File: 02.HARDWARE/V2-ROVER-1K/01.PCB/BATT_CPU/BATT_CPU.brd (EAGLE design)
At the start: 33 x 44.3 mm, 68 parts, among them J1 2314820-6, K3 FLEX_CONN, K4 FLEX6, K5 FLEX8, U1 ATSAMD21G18_QFN, U2 TPS78230DDCR, U3 TPS78230DDCR, U5 MAX9062EUK+T, U6 MAX9062EUK+T, U7 MCP6071T-E/OT, U8 SN74LVC1G19DBVR, X2 32.768

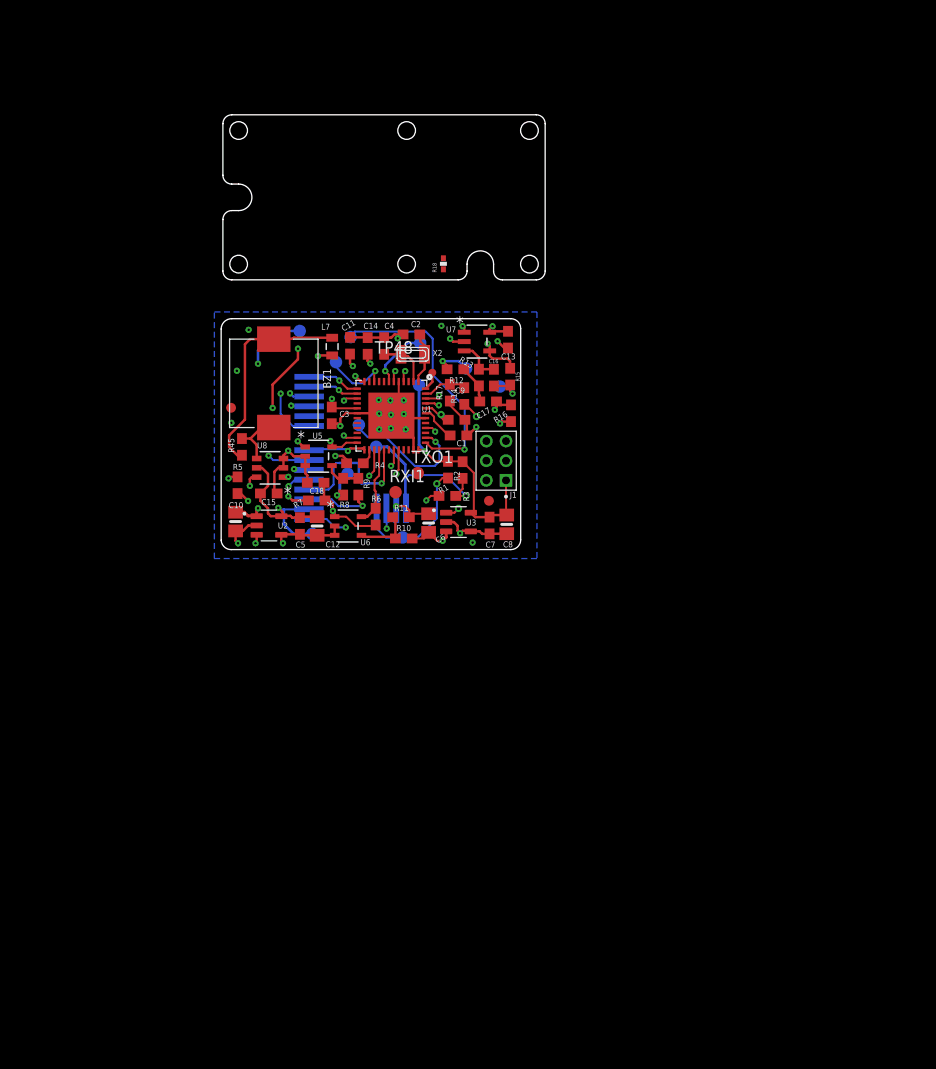
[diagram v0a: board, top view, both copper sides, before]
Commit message: Trabajo dia 31 Oct. Update
SOLO TRABAJO SOBRE ESQUEMATICO.
- Inclusion pantalla 49".
- Cambio en el diseño de la gestion de la laimentacion. Inclusion de transistor P comandado por 2 N (Boton de encendido y Señal digital CPU)
- Multiplaxado del control del DCDC y del Switch de salida, entre las señales digitales de la CPU y el comparador.
- Se añaden fajas place holder.
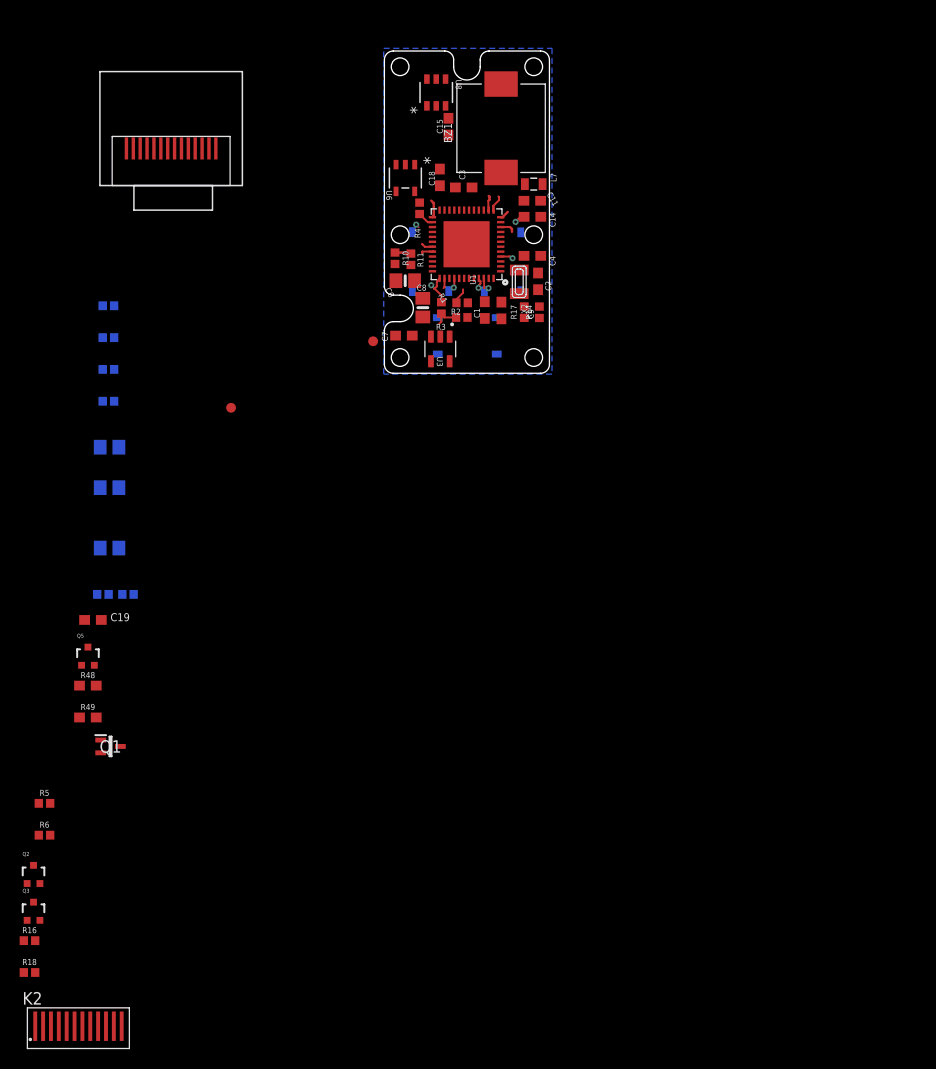
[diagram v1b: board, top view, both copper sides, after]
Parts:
- removed C10, C12: 2.2uF, microbuilder:0805-NO
- removed C5: 100n, microbuilder:0603-NO
- removed GND, IOSENSE, ISENSE_RAW, RXI, RXI1, SCL_2, SDA_2, TST_MODE, TXO, TXO1, VBUS, VCC, VCC_2, VOUTSENSE: TESTPAD_TPSQB1,27, BeagleBone_Blue_R3:TESTPAD_B1,27
- removed J1: 2314820-6, connector 2x3-2mm:TE_2314820-6
- removed K3: FLEX_CONN, Flex_3mm:FLEX4
- removed K4: FLEX6, Flex_3mm:FLEX6
- removed K5: FLEX8, Flex_3mm:FLEX8
- removed R45: 330, SparkFun-Resistors:0603
- removed TP48: TPTP08R, testpad:TP08R
- removed U2: TPS78230DDCR, TPS78230DDCR:SOT95P280X110-5N
- removed U5: MAX9062EUK+T, MAX9062:21-0057F_MXM
- removed U7: MCP6071T-E/OT, MCP6071:SOT-23-5_MC_MCH
- added C19: 100n, microbuilder:0603-NO
- added K2: FLEX6, Flex:FLEX6
- added Q1: BSS84W-7-F, BSS84W-7-F:SOT65P222X110-3N
- added Q2, Q3, Q5: 2N7002PW, SparkFun-DiscreteSemi:SOT323
- added R48: 100R, SparkFun-Resistors:0603
- added R49: 10k, SparkFun-Resistors:0603
- added S1, S2, S3: PTS526_SKG15_SMTR2_LFS, PTS526_SKG15_SMTR2_LFS:PTS526SKG15SMTR2LFS
- added U$30: 64X32_OLED_049, OLED 66 64x48:LCD_14_PINS
- C13: device microbuilder:0603-NO -> rcl:C0805
- C16, C17: value 1u -> 100n; device microbuilder:0603-NO -> rcl:C0805
- R1, R10, R14, R17, R2, R3, R4: device SparkFun-Resistors:0603 -> SparkFun-Resistors:0402
- R11: value 8.2k -> 8k2; device SparkFun-Resistors:0603 -> SparkFun-Resistors:0402
- R12: value 2.4k -> 2k2; device SparkFun-Resistors:0603 -> SparkFun-Resistors:0402
- R13: value 62k -> 100R; device SparkFun-Resistors:0603 -> SparkFun-Resistors:0402
- R15: value 2.4k -> 100R; device SparkFun-Resistors:0603 -> SparkFun-Resistors:0402
- R16: value 36k -> (none); device SparkFun-Resistors:0603 -> SparkFun-Resistors:0402
- R18: value RESISTOR0402 -> (none); device BeagleBone_Blue_R3:0402-RES -> SparkFun-Resistors:0402
- R5: value 100k -> (none); device SparkFun-Resistors:0603 -> SparkFun-Resistors:0402
- R6: value 10k -> (none); device SparkFun-Resistors:0603 -> SparkFun-Resistors:0402
- R7: value 10k -> 2k2; device SparkFun-Resistors:0603 -> SparkFun-Resistors:0402
- R8: value 120k -> 100R; device SparkFun-Resistors:0603 -> SparkFun-Resistors:0402
- R9: value 5.6k -> 2k2; device SparkFun-Resistors:0603 -> SparkFun-Resistors:0402
- moved R18 83.5 mm to (4.55, -36.4), turned to 0 degrees
- moved R16 72.7 mm to (4.55, -33.2), turned to 0 degrees
- moved R15 47.0 mm to (12.0, 2.08), flipped to the bottom, turned to 0 degrees
- moved R6 46.8 mm to (6.08, -22.4), turned to 0 degrees
- moved C13 42.0 mm to (12.7, 17.1), flipped to the bottom, turned to 0 degrees
- moved U8 41.8 mm to (46.0, 53.2), turned to 90 degrees
- moved C15 41.6 mm to (47.2, 49.7), turned to 270 degrees
- moved C17 41.3 mm to (12.7, 6.79), flipped to the bottom
- moved C16 40.7 mm to (12.7, 12.9), flipped to the bottom, turned to 0 degrees
- moved R5 37.9 mm to (6.08, -19.2), turned to 0 degrees
- moved R13 37.8 mm to (12.6, 21.7), flipped to the bottom, turned to 0 degrees
- moved U6 35.9 mm to (42.8, 44.5), turned to 270 degrees
- moved R12 35.3 mm to (12.6, 25.0), flipped to the bottom, turned to 0 degrees
- moved BZ1 34.8 mm to (52.6, 49.5), turned to 90 degrees
- moved C18 33.6 mm to (46.3, 44.5), turned to 90 degrees
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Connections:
- removed net #EN_DCDC: K5.9, U1.25
- removed net /FLAG_BATTLOW: R6.1, U1.28, U6.5
- removed net D+: U1.34
- removed net D-: U1.33
- removed net EN_VCC2: R5.2, U1.15, U2.3
- removed net FLAG_CHRG: R7.1, U1.24, U5.5
- removed net ISENSE_RAW: ISENSE_RAW.TP, K5.5, R12.2
- removed net N$11: R8.1, R9.1, U5.4
- removed net N$12: U1.39
- removed net N$14: U1.41
- removed net N$15: TP48.TP, U1.48
- removed net N$4: U1.11
- removed net N$8: C17.1, R12.1, R13.2
- removed net OP_SWITCH: K5.4, U1.29
- removed net SCL2_CPU: R4.2, U1.26
- removed net SCL_2: K3.4, R1.1, R4.1, SCL_2.TP
- removed net SDA2_CPU: R3.2, U1.27
- removed net SDA_2: K3.1, R2.1, R3.1, SDA_2.TP
- removed net USB_SEL: U1.30
- removed net VCC_2: C12.1, C13.1, C15.1, C5.1, K4.1, K5.2, U2.5, U7.5, U8.5, VCC_2.TP
- new net CPU_EN_OUT: R18.2, U1.25
- new net EN_OUT: K2.4, Q5.3, R18.1
- new net EN_VCC: Q3.1, R16.2, U1.15
- new net IN_OVC: Q5.1, R48.2, R49.2
- new net N$2: C13.1, R8.2, R9.2, S1.2
- new net N$3: C16.1, R12.2, R13.1, S2.2
- new net N$58: R48.1, U6.5
- new net N$6: Q1.1, Q2.3, Q3.3, R5.2
- new net SCL_CPU: R4.2, U1.32
- new net SDA_CPU: R3.2, U1.31
- new net S_POWER: Q2.1, R15.2, R6.2
- net !RESET: now also K2.10; no longer J1.3
- net GND: now also C17.2, C19.2, K2.2, Q2.2, Q3.2, Q5.2, R16.1, R49.1, R6.1, S1.4, S2.4, S3.4; no longer C10.2, C12.2, C5.2, GND.TP, J1.5, K3.2, K4.2, K5.3, R15.2, R5.1, R9.2, U2.2, U2.4, U5.2, U5.3, U7.2
- net IOSENSE: now also K2.8; no longer C17.2, IOSENSE.TP, R16.1, U7.1
- net N$1: now also C17.1, R7.2, S3.2; no longer R16.2, U7.4
- net N$10: now also C19.1
- net N$13: now also C6.1, Q1.2, U3.1, U3.3; no longer C16.1, R13.1, U7.3
- net N$19: no longer R45.1
- net N$22: no longer R45.2
- net RXI: now also K2.7; no longer RXI.TP, RXI1.TP
- net SCL: now also R1.1, R4.1; no longer K4.4, K5.7, U1.32
- net SDA: now also R2.1, R3.1; no longer K4.3, K5.1, U1.31
- net SWCLK: now also K2.6; no longer J1.4
- net SWDIO: now also K2.5; no longer J1.2
- net S_DOWN: now also R13.2; no longer K4.6
- net S_UP: now also R8.1; no longer K4.5
- net TST_MODE: no longer TST_MODE.TP
- net TXO: no longer TXO.TP, TXO1.TP
- net VBUS: now also K2.3, Q1.3, R5.1, R7.1; no longer C10.1, C6.1, K3.3, R8.2, U2.1, U3.1, U3.3, VBUS.TP
- net VCC: now also C15.1, K2.1, R12.1, R9.1, U8.5; no longer J1.1, R6.2, R7.2, U5.1, VCC.TP
- net VOUTSENSE: now also K2.9; no longer K5.8, VOUTSENSE.TP
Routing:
- net GND: track 77.5 -> 0.00 mm, vias 27 -> 0
- net VCC: track 45.6 -> 0.00 mm, vias 7 -> 0
- net ISENSE_RAW: track 41.5 -> 0.00 mm, vias 4 -> 0
- net SDA_CPU: track 0.00 -> 37.5 mm, vias 0 -> 2
- net SCL_2: track 28.9 -> 0.00 mm, vias 2 -> 0
- net VCC_2: track 28.4 -> 0.00 mm, vias 3 -> 0
- net SDA: track 30.5 -> 2.84 mm, vias 3 -> 0
- net TXO: track 25.7 -> 1.32 mm, vias 1 -> 0
- net SCL_CPU: track 0.00 -> 23.8 mm
- net EN_VCC2: track 23.2 -> 0.00 mm, vias 3 -> 0
- net N$19: track 21.9 -> 0.00 mm
- net SDA_2: track 21.5 -> 0.00 mm, vias 1 -> 0
- net EN_VCC: track 0.00 -> 19.4 mm
- net VBUS: track 64.1 -> 47.3 mm, vias 6 -> 0
- net OP_SWITCH: track 15.1 -> 0.00 mm, vias 1 -> 0
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- removed copper zone on layer 2, net VCC_2
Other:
- board size 33 x 44.3 mm -> 16.8 x 32.8 mm
- board text removed: "BATT_CPU v5 Nov21"

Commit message: Modificacion Ruteado CPU
Se añade la version 1 de las dimensiones del PCB y se posicionan los componentes sin ruteado.
FALTA: Circuito acondicionamiento Display .
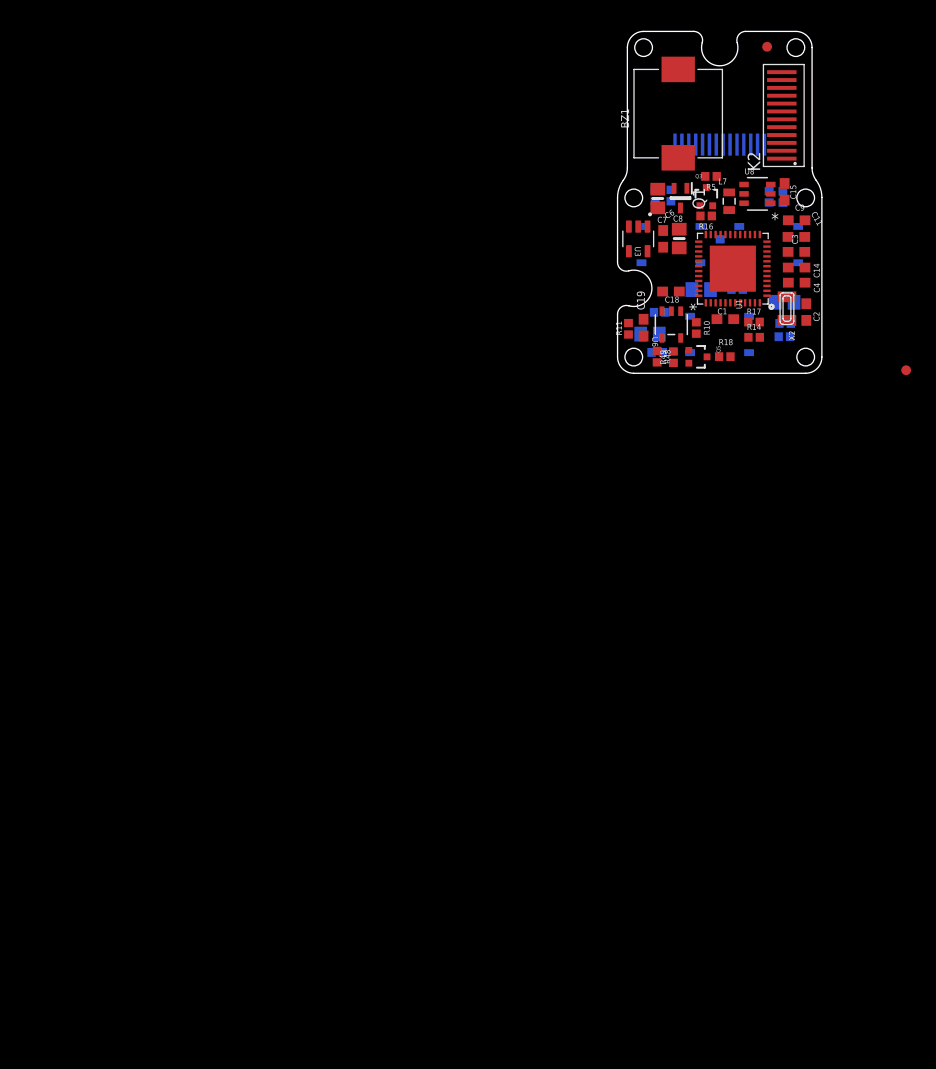
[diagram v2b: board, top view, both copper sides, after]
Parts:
- removed Q2: 2N7002PW, SparkFun-DiscreteSemi:SOT323
- removed R6: (no value), SparkFun-Resistors:0402
- R48: device SparkFun-Resistors:0603 -> SparkFun-Resistors:0402
- R49: value 10k -> 10K; device SparkFun-Resistors:0603 -> SparkFun-Resistors:0402
- moved K2 116.5 mm to (80.9, 48.9), turned to 90 degrees
- moved R16 100.9 mm to (73.4, 40.6), turned to 180 degrees
- moved Q3 99.9 mm to (73.4, 42.6)
- moved R18 94.5 mm to (75.3, 26.3)
- moved R5 93.1 mm to (73.9, 44.6), turned to 180 degrees
- moved Q1 80.5 mm to (70.8, 42.4), turned to 270 degrees
- moved C16 71.3 mm to (81.4, 31.8), turned to 180 degrees
- moved R49 70.0 mm to (70.1, 26.2), turned to 90 degrees
- moved Q5 69.2 mm to (72.6, 26.3), turned to 270 degrees
- moved R13 69.1 mm to (81.4, 28.3), turned to 180 degrees
- moved R12 69.0 mm to (81.5, 29.7)
- moved U$35 68.8 mm to (93.8, 24.9)
- moved R48 66.9 mm to (68.4, 26.3), turned to 270 degrees
- moved U$30 64.9 mm to (79.4, 46.7), flipped to the bottom
- moved R8 64.0 mm to (76.6, 33.1)
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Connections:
- net CPU_EN_OUT renamed CPU_EN_DCDC
- net EN_OUT renamed EN_DCDC
- net EN_VCC renamed EN_VCC_2
- removed net N$13: C6.1, Q1.2, U3.1, U3.3
- new net N$4: U1.26
- new net OP_SWITCH: K2.11
- new net VCC_2: K2.12, Q1.2
- net GND: no longer Q2.2, R6.1
- net N$6: no longer Q2.3
- net S_POWER: no longer Q2.1, R6.2
- net VBUS: now also C6.1, U3.1, U3.3; no longer Q1.3, R5.1
- net VCC: now also Q1.3, R5.1
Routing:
- net VBUS: track 47.3 -> 0.00 mm
- net SDA_CPU: track 37.5 -> 0.00 mm, vias 2 -> 0
- net VOUTSENSE: track 23.9 -> 0.00 mm
- net SCL_CPU: track 23.8 -> 0.00 mm
- net N$17: track 21.1 -> 0.00 mm
- net EN_VCC_2: track 19.4 -> 0.00 mm
- net IOSENSE: track 18.8 -> 0.00 mm
- net SWDIO: track 16.7 -> 0.00 mm, vias 1 -> 0
- net SCL: track 14.9 -> 0.00 mm
- net !RESET: track 13.8 -> 0.00 mm, vias 1 -> 0
- net TST_MODE: track 11.9 -> 0.00 mm
- net BUZZER: track 8.86 -> 0.00 mm
- net SWCLK: track 6.44 -> 0.00 mm, vias 1 -> 0
- net AREF: track 6.19 -> 0.00 mm, vias 2 -> 0
- net SDA: track 2.84 -> 0.00 mm
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- removed copper zone on layer 15, net GND
- removed copper zone on layer 16, net GND
- removed copper zone on layer 2, net GND
- removed copper zone on layer 2, net VCC
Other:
- board size 16.8 x 32.8 mm -> 20.8 x 34.8 mm

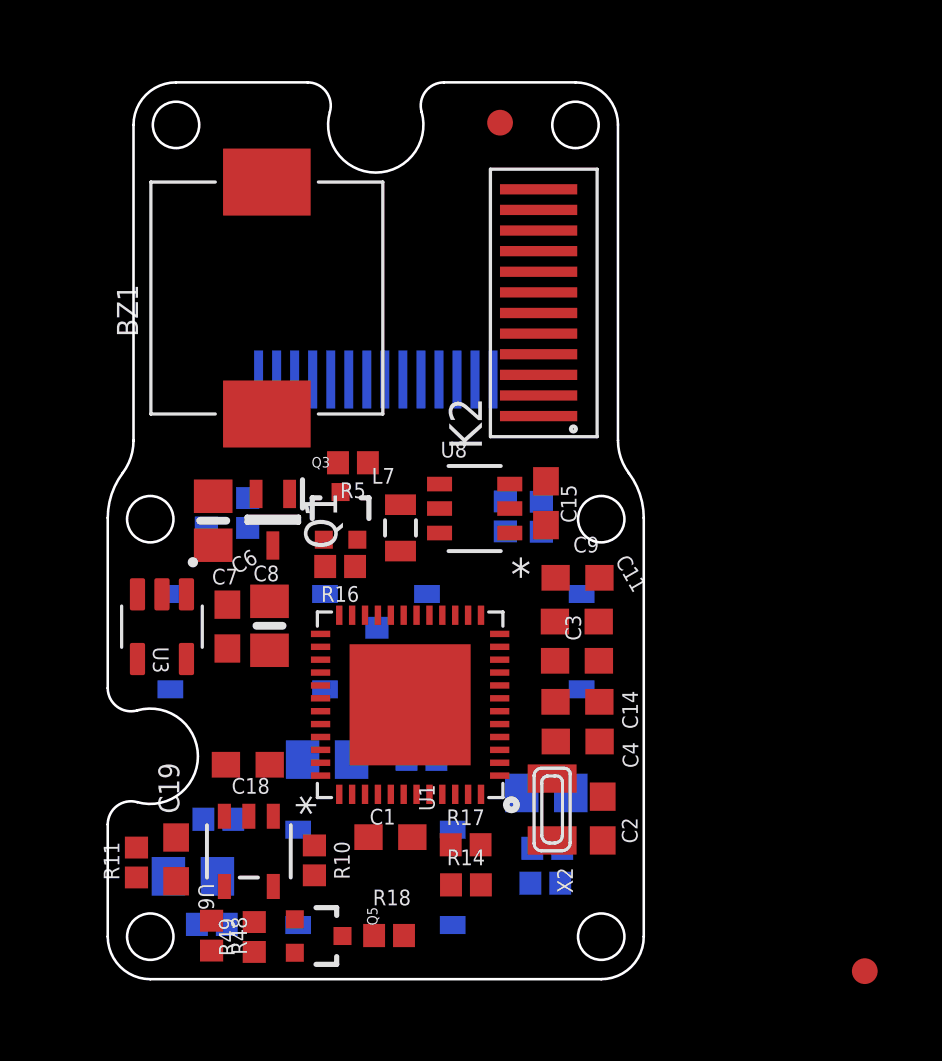
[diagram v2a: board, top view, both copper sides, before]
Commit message: Update CPU PCB.
Routeado terminado v1. PENDIENTE DE REVISION.
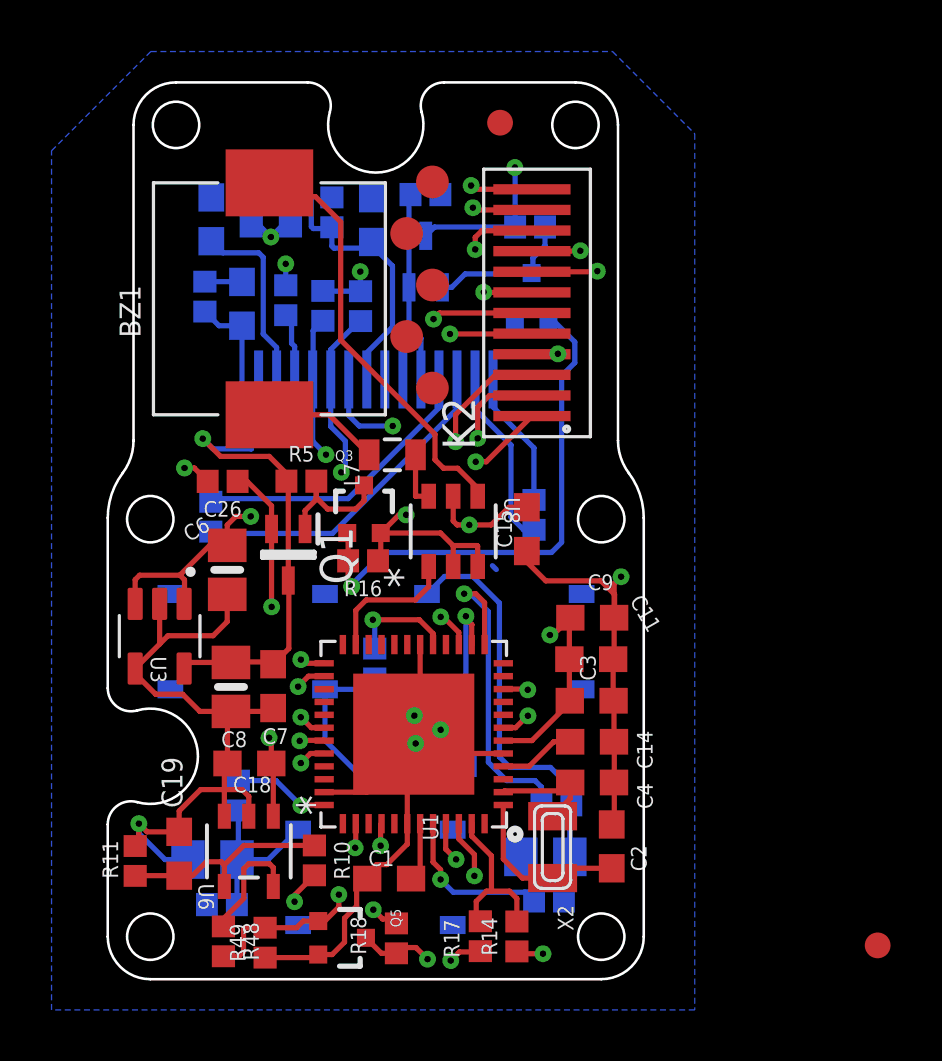
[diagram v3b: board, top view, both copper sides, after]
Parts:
- added C10, C24, C25, C26, C5: 0.1uF, SparkFun-Capacitors:0402
- added C12, C23: 1.0uF, SparkFun-Capacitors:0402
- added C20: 2.2uF, SparkFun-Capacitors:0603
- added C21, C22: 4.7uF, SparkFun-Capacitors:0603
- added Q2: BSS84W-7-F, BSS84W-7-F:SOT65P222X110-3N
- added Q4: 2N7002PW, SparkFun-DiscreteSemi:SOT323
- added R6: 4K7, SparkFun-Resistors:0402
- added VBUS, VBUS1, VBUS2, VBUS3, VBUS4: TESTPAD_TPSQB1,27, BeagleBone_Blue_R3:TESTPAD_B1,27
- R1, R2: value 2k2 -> 4K7
- R3: value 100R -> 560K
- R4: value 100R -> (none)
- moved R4 15.6 mm to (80.8, 53.8), turned to 180 degrees
- moved R3 12.0 mm to (71.3, 50.9), turned to 270 degrees
- moved R2 11.8 mm to (72.8, 50.7)
- moved R1 10.00 mm to (74.2, 50.7)
- moved R7 5.11 mm to (69.5, 31.7), turned to 270 degrees
- moved R17 3.60 mm to (78.9, 26.2), turned to 90 degrees
- moved R15 3.31 mm to (68.8, 27.5)
- moved R13 3.08 mm to (81.8, 31.4), turned to 0 degrees
- moved C7 2.92 mm to (70.8, 36.0), turned to 270 degrees
- moved L7 2.85 mm to (75.5, 44.9), turned to 180 degrees
- moved R14 2.81 mm to (80.3, 26.2), turned to 90 degrees
- moved C8 2.80 mm to (69.2, 35.9), turned to 270 degrees
- moved C16 2.48 mm to (81.4, 29.3), turned to 0 degrees
- moved R5 2.13 mm to (71.9, 43.9), turned to 0 degrees
- moved R12 2.04 mm to (81.5, 27.6), turned to 180 degrees
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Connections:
- removed net IN_OVC: Q5.1, R48.2, R49.2
- removed net SCL_CPU: R4.2, U1.32
- removed net SDA_CPU: R3.2, U1.31
- new net !RES: C24.1, R6.1, U$30.!RES
- new net C1N: C23.1, U$30.C1N
- new net C1P: C23.2, U$30.C1P
- new net C2N: C12.1, U$30.C2N
- new net C2P: C12.2, U$30.C2P
- new net IN_UVLO: Q5.1, R48.2, R49.2, U1.30
- new net IREF: R3.2, U$30.IREF
- new net N$11: U1.34
- new net N$12: U1.41
- new net N$13: U1.48
- new net N$14: U1.33
- new net N$8: U1.39
- new net VBAT_LCD: C25.1, Q2.2, U$30.VBAT
- new net VCOMH: C20.1, U$30.VCOMH
- new net VDD: C10.1, C22.1, R6.2, U$30.VDD
- new net VSS: U$30.VSS
- net EN_VCC_2: now also Q4.1
- net GND: now also C10.2, C20.2, C21.2, C22.2, C24.2, C25.2, C26.2, C5.2, Q4.2, R3.1
- net N$4: now also Q2.1, Q4.3, R4.2; no longer U1.26
- net OP_SWITCH: now also U1.26
- net SCL: now also U$30.SCL, U1.32; no longer R4.1
- net SDA: now also U$30.SDA, U1.31; no longer R3.1
- net VBUS: now also Q2.3, R4.1; no longer R7.1
- net VCC: now also C21.1, C5.1, R7.1, U$30.VCC; no longer C15.1, C18.1, R1.2, R2.2, U6.1, U8.5
- net VCC_2: now also C15.1, C18.1, C26.1, R1.2, R2.2, U6.1, U8.5
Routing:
- net GND: track 0.00 -> 83.7 mm, vias 0 -> 10
- net VBUS: track 0.00 -> 75.9 mm, vias 0 -> 5
- net VCC: track 0.00 -> 61.0 mm, vias 0 -> 6
- net VCC_2: track 0.00 -> 50.1 mm, vias 0 -> 5
- net SWCLK: track 0.00 -> 34.1 mm, vias 0 -> 2
- net SWDIO: track 0.00 -> 33.6 mm, vias 0 -> 2
- net EN_DCDC: track 0.00 -> 32.6 mm, vias 0 -> 2
- net !RESET: track 0.00 -> 32.3 mm, vias 0 -> 2
- net RXI: track 0.00 -> 30.3 mm, vias 0 -> 2
- net OP_SWITCH: track 0.00 -> 29.5 mm, vias 0 -> 2
- net EN_VCC_2: track 0.00 -> 25.8 mm, vias 0 -> 2
- net IOSENSE: track 0.00 -> 22.4 mm, vias 0 -> 2
- net VOUTSENSE: track 0.00 -> 20.9 mm, vias 0 -> 2
- net SCL: track 0.00 -> 20.0 mm, vias 0 -> 2
- net SDA: track 0.00 -> 18.4 mm, vias 0 -> 2
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- added copper zone on layer 1, net GND
- added copper zone on layer 15, net GND
- added copper zone on layer 16, net GND
- added copper zone on layer 2, net VCC
